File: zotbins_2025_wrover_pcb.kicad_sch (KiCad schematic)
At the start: 26 parts, among them J1 FFC2B28-24-G, J5 DCJ200-10-A-XX-K_REVA, J6 Conn_01x30_Pin, U1 ESP32-WROVER-E/IE-DEVKIT-C, U2 MCP23017_SP, U3 XC6206P122MR-G, U4 XC6206P282PR-G, U5 LM7805_TO220

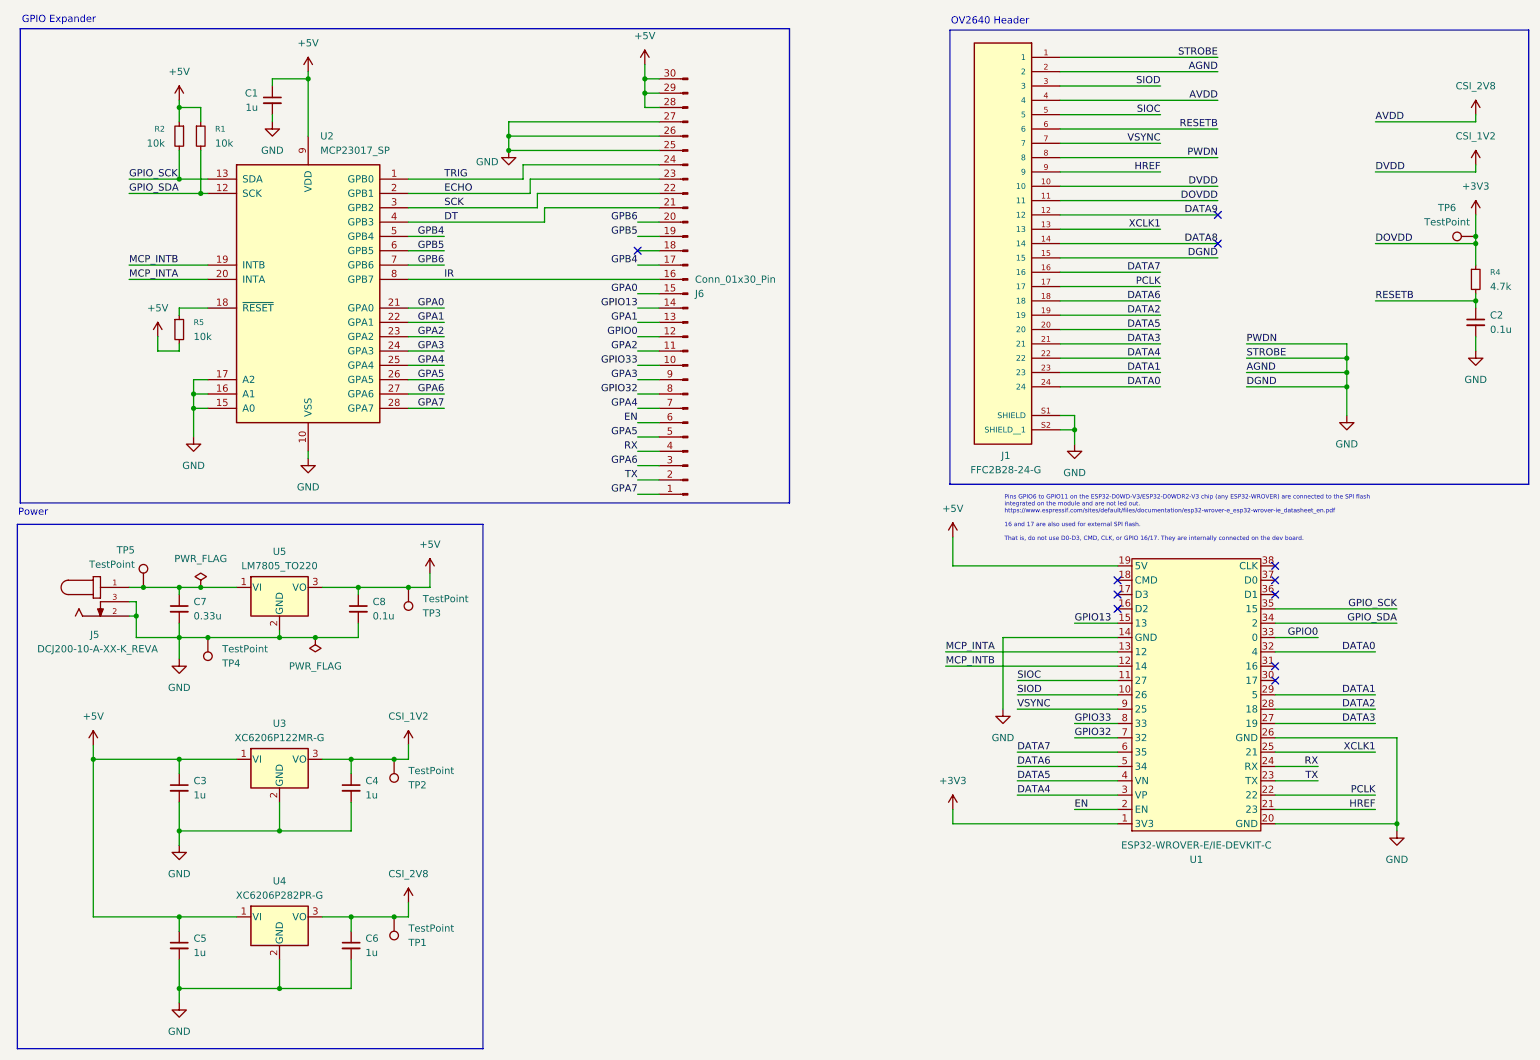
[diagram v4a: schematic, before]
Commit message: resolved ERC checks, footprint incompatibilities, symbol library not found errors; 3 ERC violations surpressed intentionally
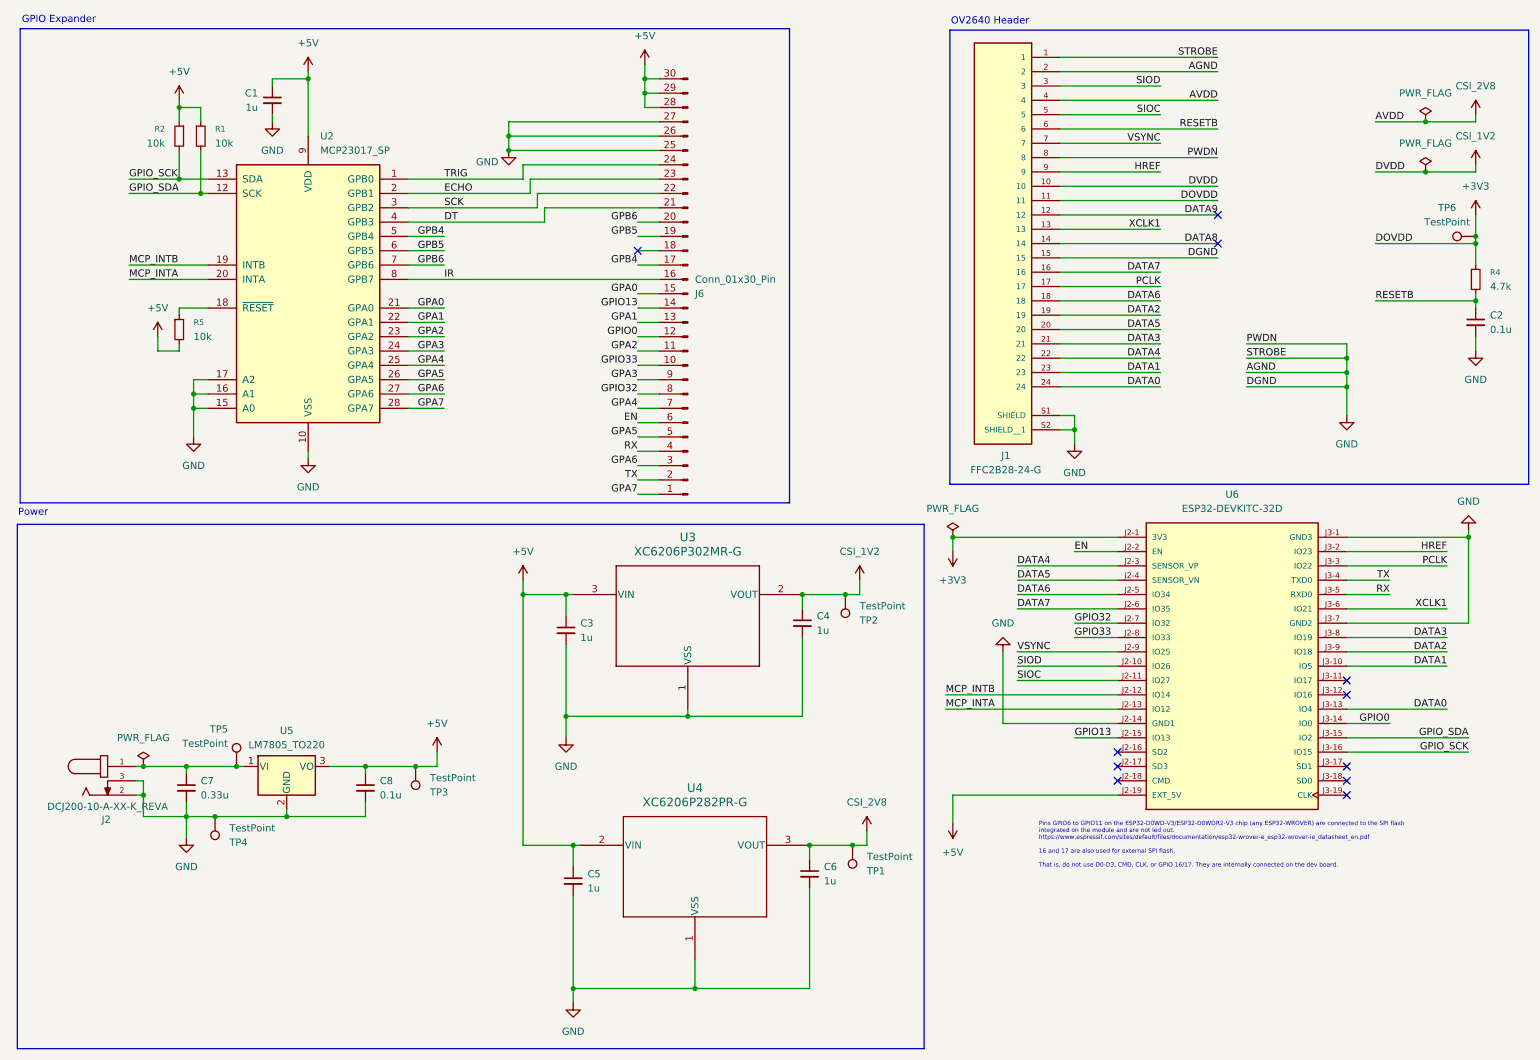
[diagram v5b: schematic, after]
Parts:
- removed J5: DCJ200-10-A-XX-K_REVA, Connector_BarrelJack:GCT_DCJ200-10-A-XX-K_REVA, symbol Converter_DCDC:DCJ200-10-A-XX-K_REVA
- removed U1: ESP32-WROVER-E/IE-DEVKIT-C, MCU_Development_Board:MODULE_ESP32-DEVKITC-32D, symbol wrover-ie-lib:ESP32-WROVER-E/IE-DEVKIT-C
- removed U3: XC6206P122MR-G, Package_TO_SOT_SMD:SOT-23, symbol Regulator_Linear:XC6206P122MR-G
- removed U4: XC6206P282PR-G, Package_TO_SOT_SMD:SOT-23, symbol Regulator_Linear:XC6206P282PR-G
- added J2: DCJ200-10-A-XX-K_REVA, Library:GCT_DCJ200-10-A-XX-K_REVA, symbol DCJ200-10-A-XX-K_REVA:DCJ200-10-A-XX-K_REVA
- added U3: XC6206P302MR-G, XC6206P302MR_G:SOT-23_TOR, symbol 2025-10-20_17-16-44:XC6206P302MR-G
- added U4: XC6206P282PR-G, XC6206P282PR_G:SOT-89_TOR, symbol 2025-10-20_17-19-37:XC6206P282PR-G
- added U6: ESP32-DEVKITC-32D, ESP32-DEVKITC-32D:MODULE_ESP32-DEVKITC-32D, symbol ESP32-DEVKITC-32D:ESP32-DEVKITC-32D
- J1: footprint Connector_FFC-FPC:GCT_FFC2B28-24-G -> Library:GCT_FFC2B28-24-G
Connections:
- net +3V3: now also U6.J2-1 (3V3)
- net +5V: now also U3.3 (VIN), U4.2 (VIN), U6.J2-19 (EXT_5V)
- net CSI_1V2: now also U3.2 (VOUT)
- net CSI_2V8: now also U4.3 (VOUT)
- net DATA0: now also U6.J3-13 (IO4)
- net DATA1: now also U6.J3-10 (IO5)
- net DATA2: now also U6.J3-9 (IO18)
- net DATA3: now also U6.J3-8 (IO19)
- net DATA4: now also U6.J2-3 (SENSOR_VP)
- net DATA5: now also U6.J2-4 (SENSOR_VN)
- net DATA6: now also U6.J2-5 (IO34)
- net DATA7: now also U6.J2-6 (IO35)
- net EN: now also U6.J2-2 (EN)
- net GND: now also J2.2, J2.3, U3.1 (VSS), U4.1 (VSS), U6.J2-14 (GND1), U6.J3-1 (GND3), U6.J3-7 (GND2)
- net GPIO0: now also U6.J3-14 (IO0)
- net GPIO13: now also U6.J2-15 (IO13)
- net GPIO32: now also U6.J2-7 (IO32)
- net GPIO33: now also U6.J2-8 (IO33)
- net GPIO_SCK: now also U6.J3-16 (IO15)
- net GPIO_SDA: now also U6.J3-15 (IO2)
- net HREF: now also U6.J3-2 (IO23)
- net MCP_INTA: now also U6.J2-13 (IO12)
- net MCP_INTB: now also U6.J2-12 (IO14)
- net PCLK: now also U6.J3-3 (IO22)
- net RX: now also U6.J3-5 (RXD0)
- net SIOC: now also U6.J2-11 (IO27)
- net SIOD: now also U6.J2-10 (IO26)
- net TX: now also U6.J3-4 (TXD0)
- net VSYNC: now also U6.J2-9 (IO25)
- net XCLK1: now also U6.J3-6 (IO21)
- net at C7.1, TP5.1, U5.1 (VI): now also J2.1
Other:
- moved on the sheet: C7, C8, TP3, TP4, TP5, U5
